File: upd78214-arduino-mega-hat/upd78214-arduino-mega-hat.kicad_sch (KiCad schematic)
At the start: 17 parts, among them J1 Power, J2 PWM, J3 Analog, J4 PWM, J5 Analog, J6 Communication, J7 Digital, SW1 SW_SPST, SW2 SW_SPDT, U1 upd78214-64p-qfp, Y1 4-12MHz

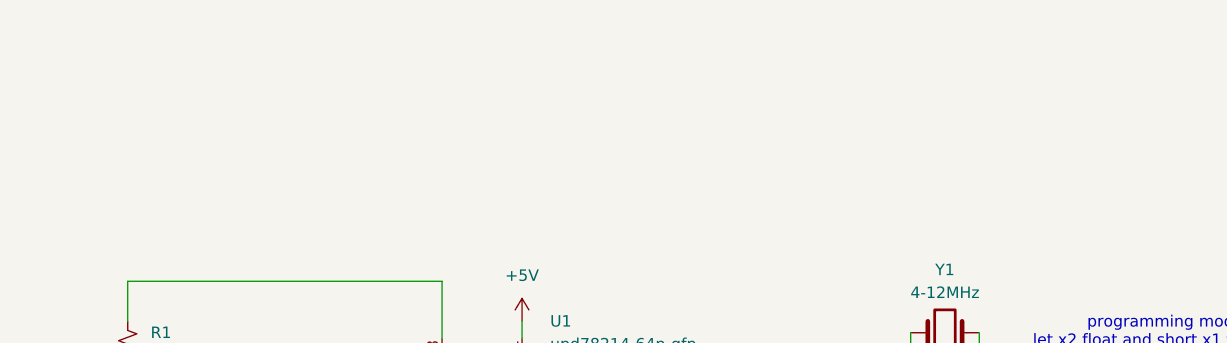
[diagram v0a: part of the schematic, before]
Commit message: Correct Shield to use right footprint, have jumper pins
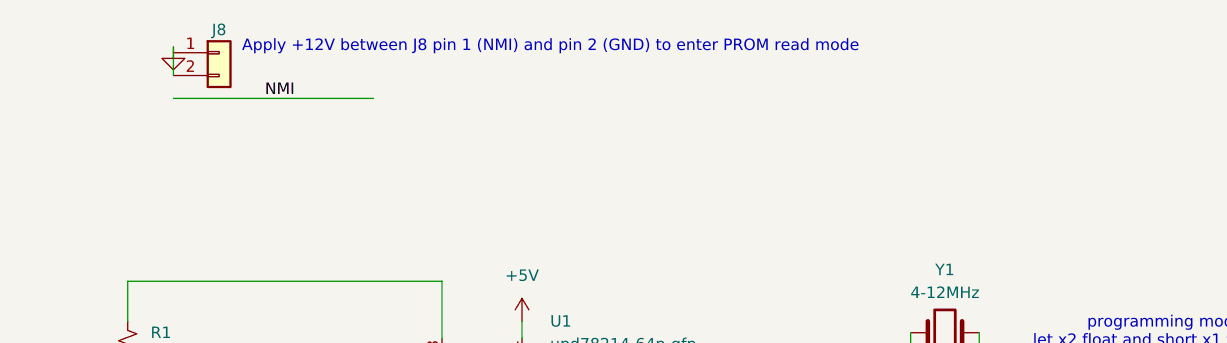
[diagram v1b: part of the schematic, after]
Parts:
- added J8: Conn_01x02, Connector_PinHeader_2.54mm:PinHeader_1x02_P2.54mm_Vertical, symbol Connector_Generic:Conn_01x02
- U1: footprint Package_QFP:TQFP-64_14x14mm_P0.8mm -> NEC:QFP-64_14x14_Pitch0.8mm
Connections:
- net GND: now also J8.2 (Pin_2)
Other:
- note added: "Apply +12V between J8 pin 1 (NMI) and pin 2 (GND) to enter PROM read mode"
